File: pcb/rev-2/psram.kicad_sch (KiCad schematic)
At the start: 7 parts, among them U11 APS1604M-3SQR-ZR

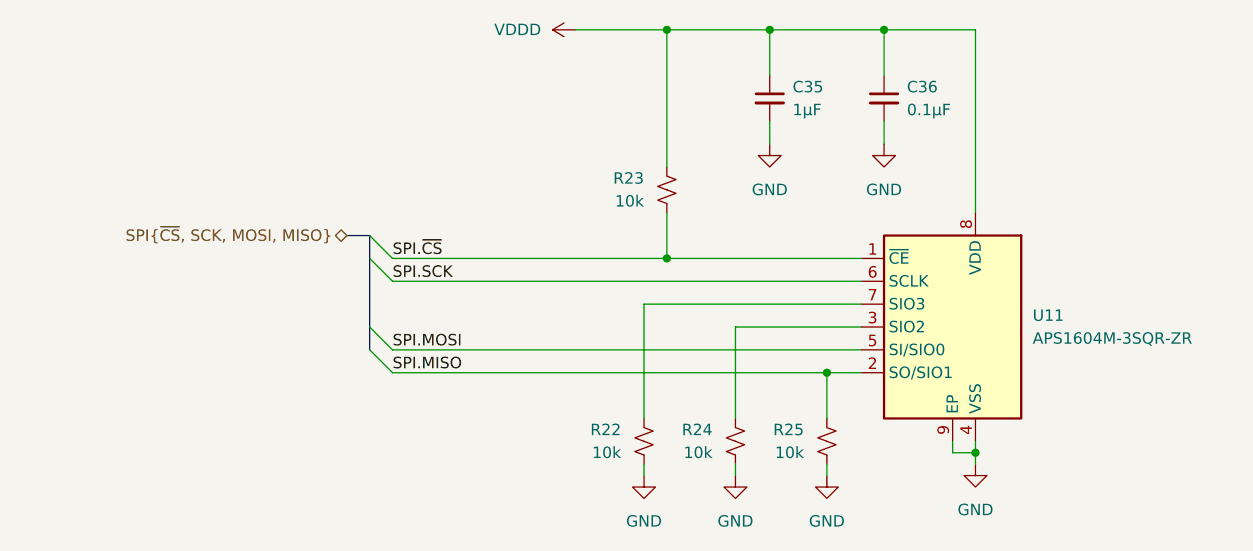
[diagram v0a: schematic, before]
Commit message: pcb: full rev-2 layout
Mostly finished layout for the rev-2 board
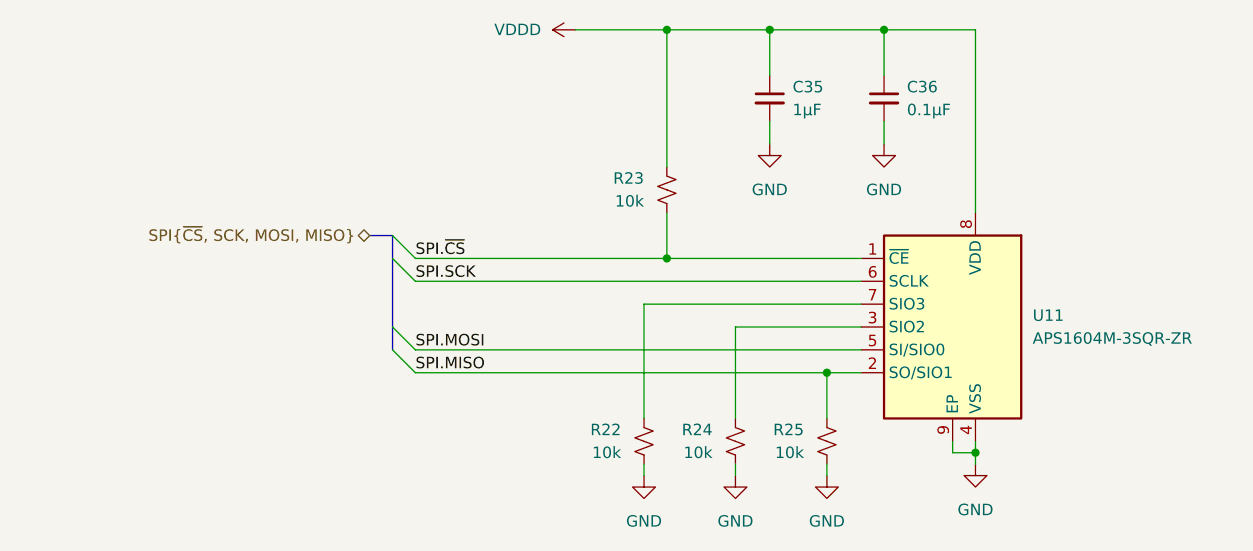
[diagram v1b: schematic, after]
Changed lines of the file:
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@@
 	)
 	(bus_entry
-		(at 121.92 82.55)
+		(at 124.46 82.55)
 		(size -2.54 -2.54)
 		(stroke
@@
 	)
 	(bus_entry
-		(at 121.92 92.71)
+		(at 124.46 92.71)
 		(size -2.54 -2.54)
 		(stroke
@@
 	)
 	(bus_entry
-		(at 121.92 80.01)
+		(at 124.46 80.01)
 		(size -2.54 -2.54)
 		(stroke
@@
 	)
 	(bus_entry
-		(at 121.92 90.17)
+		(at 124.46 90.17)
 		(size -2.54 -2.54)
 		(stroke
@@
 	(wire
 		(pts
-			(xy 121.92 82.55) (xy 173.99 82.55)
+			(xy 124.46 82.55) (xy 173.99 82.55)
 		)
 		(stroke
@@
 	(bus
 		(pts
-			(xy 119.38 77.47) (xy 116.84 77.47)
+			(xy 121.92 77.47) (xy 119.38 77.47)
 		)
 		(stroke
@@
 	(bus
 		(pts
-			(xy 119.38 80.01) (xy 119.38 77.47)
+			(xy 121.92 80.01) (xy 121.92 77.47)
 		)
 		(stroke
@@
 	(wire
 		(pts
-			(xy 121.92 92.71) (xy 170.18 92.71)
+			(xy 124.46 92.71) (xy 170.18 92.71)
 		)
 		(stroke
@@
 	(bus
 		(pts
-			(xy 119.38 87.63) (xy 119.38 90.17)
+			(xy 121.92 87.63) (xy 121.92 90.17)
 		)
 		(stroke
@@
 	(bus
 		(pts
-			(xy 119.38 87.63) (xy 119.38 80.01)
+			(xy 121.92 87.63) (xy 121.92 80.01)
 		)
 		(stroke
@@
 	(wire
 		(pts
-			(xy 121.92 90.17) (xy 173.99 90.17)
+			(xy 124.46 90.17) (xy 173.99 90.17)
 		)
 		(stroke
@@
 	(wire
 		(pts
-			(xy 121.92 80.01) (xy 152.4 80.01)
+			(xy 124.46 80.01) (xy 152.4 80.01)
 		)
 		(stroke
@@
 	)
 	(label "SPI.MISO"
-		(at 121.92 92.71 0)
+		(at 124.46 92.71 0)
 		(fields_autoplaced yes)
 		(effects
@@
 	)
 	(label "SPI.MOSI"
-		(at 121.92 90.17 0)
+		(at 124.46 90.17 0)
 		(fields_autoplaced yes)
 		(effects
@@
 	)
 	(label "SPI.SCK"
-		(at 121.92 82.55 0)
+		(at 124.46 82.55 0)
 		(fields_autoplaced yes)
 		(effects
@@
 	)
 	(label "SPI.~{CS}"
-		(at 121.92 80.01 0)
+		(at 124.46 80.01 0)
 		(fields_autoplaced yes)
 		(effects
@@
 	(hierarchical_label "SPI{~{CS}, SCK, MOSI, MISO}"
 		(shape bidirectional)
-		(at 116.84 77.47 180)
-		(fields_autoplaced yes)
-		(effects
+		(at 119.38 77.47 180)
+		(fields_autoplaced yes)
+		(effects

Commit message: pcb: minor schematic cleanup
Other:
- title: (none) -> PSRAM
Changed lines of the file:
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@@
 	(generator_version "8.0")
 	(paper "A4")
+	(title_block
+		(title "PSRAM")
+	)
 	(junction
 		(at 170.18 92.71)

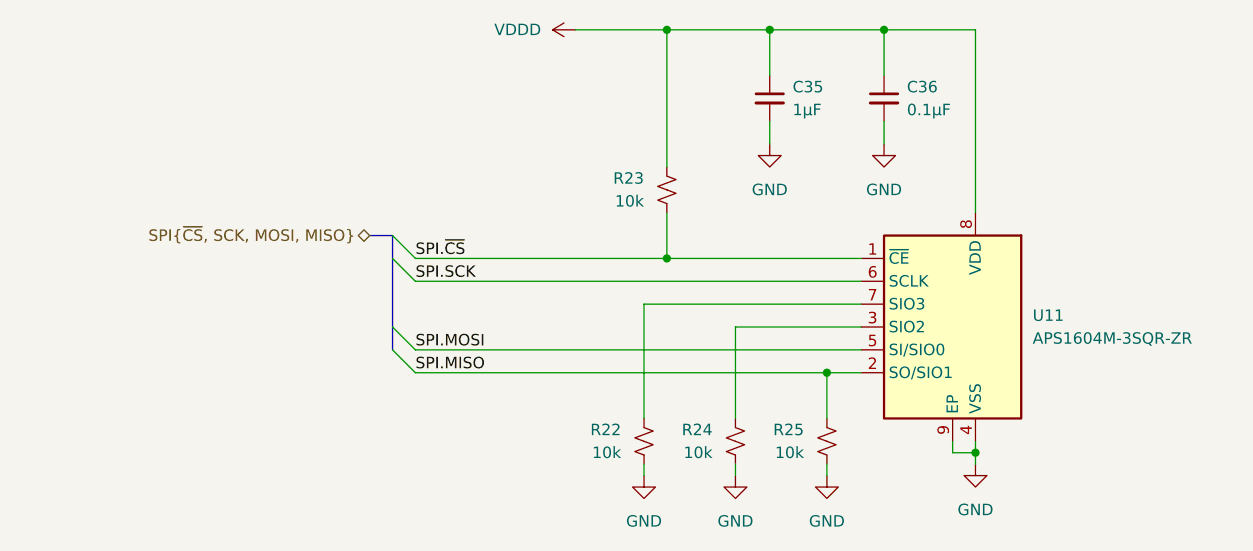
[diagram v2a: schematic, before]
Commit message: pcb: update
Mostly downsize several decoupling capacitors to save space
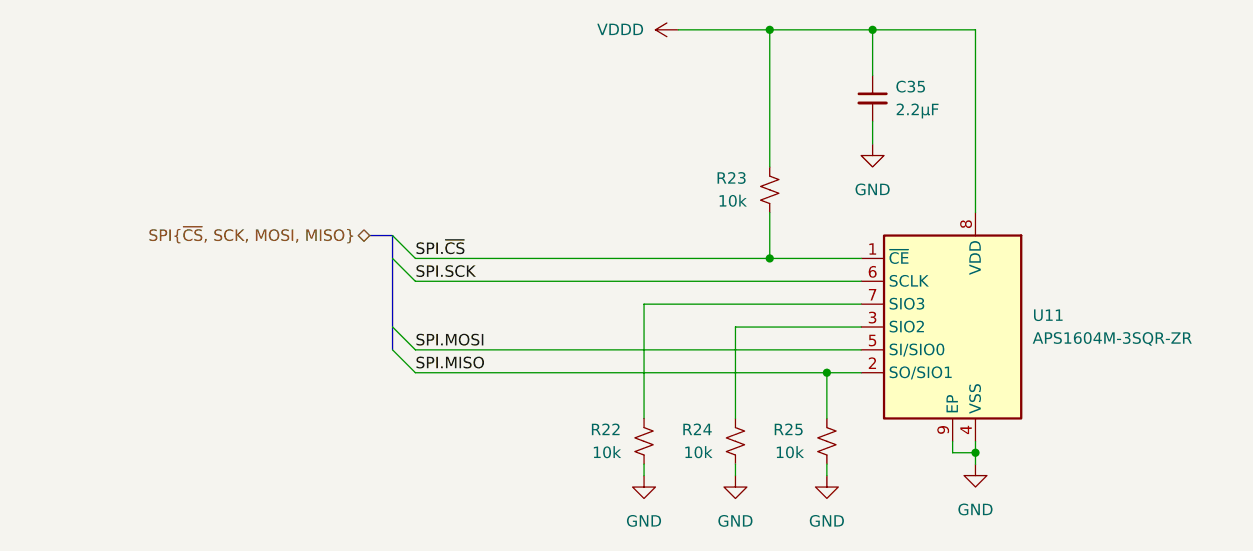
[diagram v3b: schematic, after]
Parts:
- removed C36: 0.1µF, zeus-le:C_0402_1005Metric_Silkscreen_Clearance, symbol Device:C_Small
- C35: value 1µF -> 2.2µF; footprint Capacitor_SMD:C_0603_1608Metric -> zeus-le:C_0402_1005Metric_Silkscreen_Clearance; manf# CL10B105KP8NNNC -> GRM155R61A225ME01D
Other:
- moved on the sheet: C35, R23

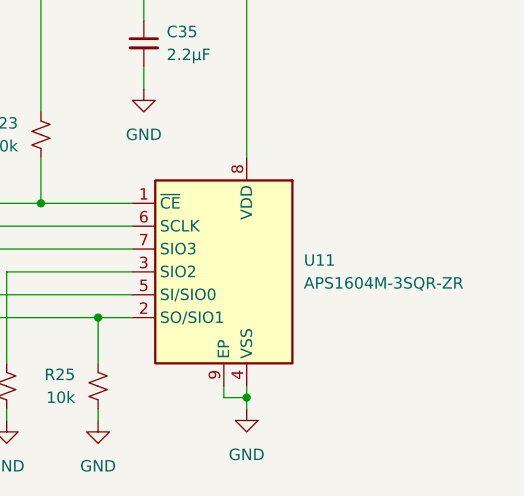
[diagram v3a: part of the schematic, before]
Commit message: Increase PSRAM size to 64Mbit
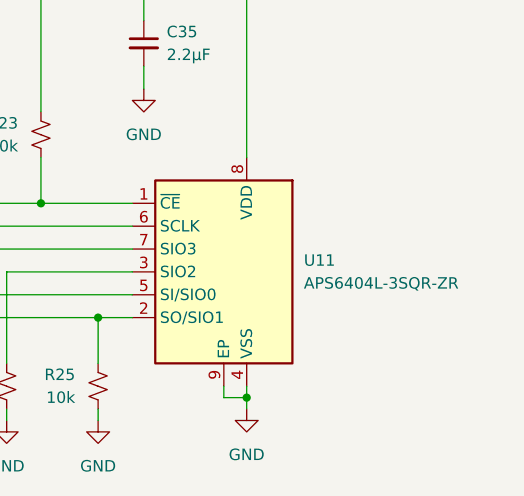
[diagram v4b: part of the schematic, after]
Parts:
- U11: value APS1604M-3SQR-ZR -> APS6404L-3SQR-ZR
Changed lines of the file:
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@@
 			)
 		)
-		(property "Value" "APS1604M-3SQR-ZR"
+		(property "Value" "APS6404L-3SQR-ZR"
 			(at 193.04 88.8999 0)
 			(effects
@@
 			)
 		)
-		(property "Datasheet" "https://www.apmemory.com/wp-content/uploads/APM_PSRAM_QSPI-APS1604M-3SQR-v2.7-PKG.pdf"
+		(property "Datasheet" "https://www.mouser.com/datasheet/2/1127/APM_PSRAM_QSPI_APS6404L_3SQR_v2_3_PKG-1954826.pdf"
 			(at 194.31 74.93 0)
 			(effects
@@
 			)
 		)
-		(property "Description" "16 Mbit serial pseudo SRAM device organized as 2Mx8 bits, 3.3 VDD, USON-8"
+		(property "Description" "64 Mbit serial pseudo SRAM device organized as 8Mx8 bits, 3.3 VDD, USON-8"
 			(at 184.15 87.63 0)
 			(effects

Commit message: Update PCBs
* Update to KiCad 10
* Update footprint for nRF53 module based on 1.01 datasheet with
  actually readable mechanical drawing
* Add 3D model for production nRF53 module
* Remove overlapping silkscreen on rev-1 with production nRF53 module
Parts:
- U11: manf# (none) -> APS6404L-3SQR-ZR
